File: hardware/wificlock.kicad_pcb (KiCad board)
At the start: 4 copper layers, 71.8 x 30.5 mm, 41 parts, among them J1 USB_C_Receptacle_USB2.0, Q1 AO3402, Q2 AO3402, Q3 AO3402, Q4 AO3402, SW1 SW_SPST, SW2 SW_SPST, SW3 SW_SPST, U1 CH340C/G, U2 ESP-12F, U3 ME6211C33M5G, U4 HT16K33-20SOP, U5 KW4-56NCLB-P, Y1 12MHz

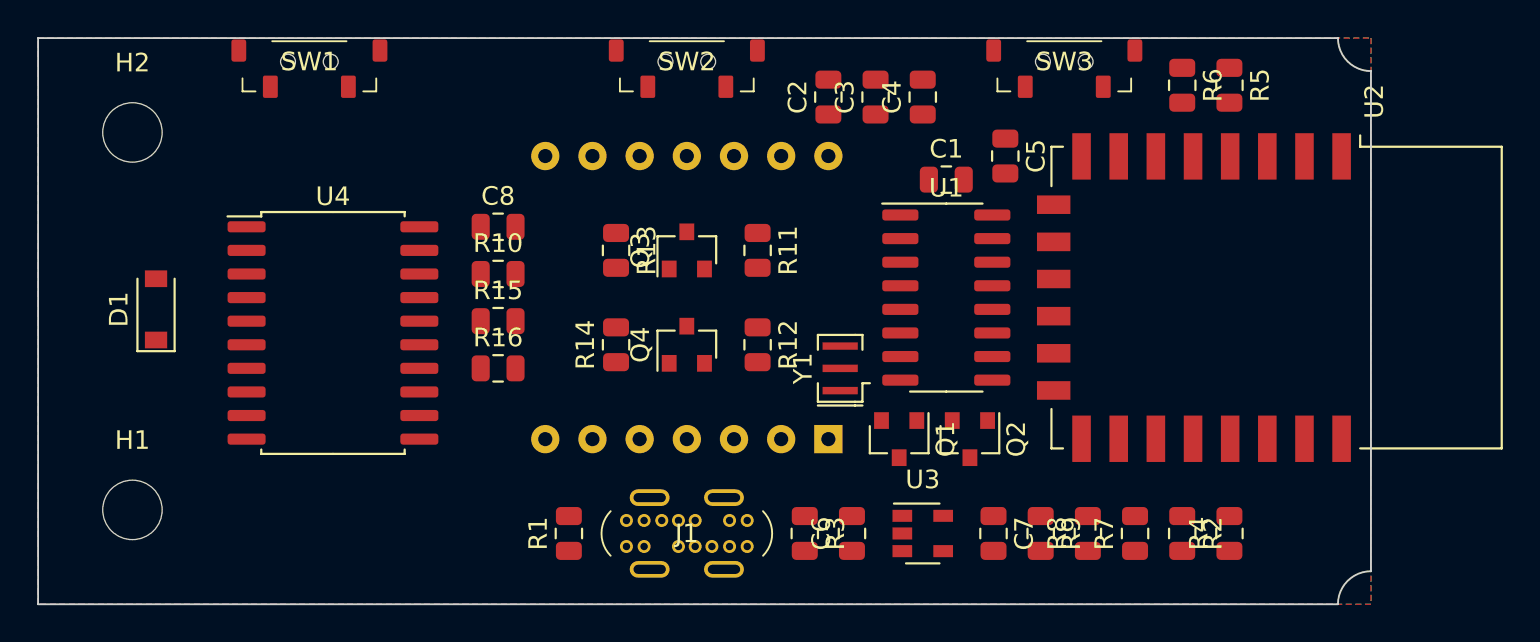
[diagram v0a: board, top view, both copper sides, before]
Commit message: manually route IC decoupling and some other critical traces
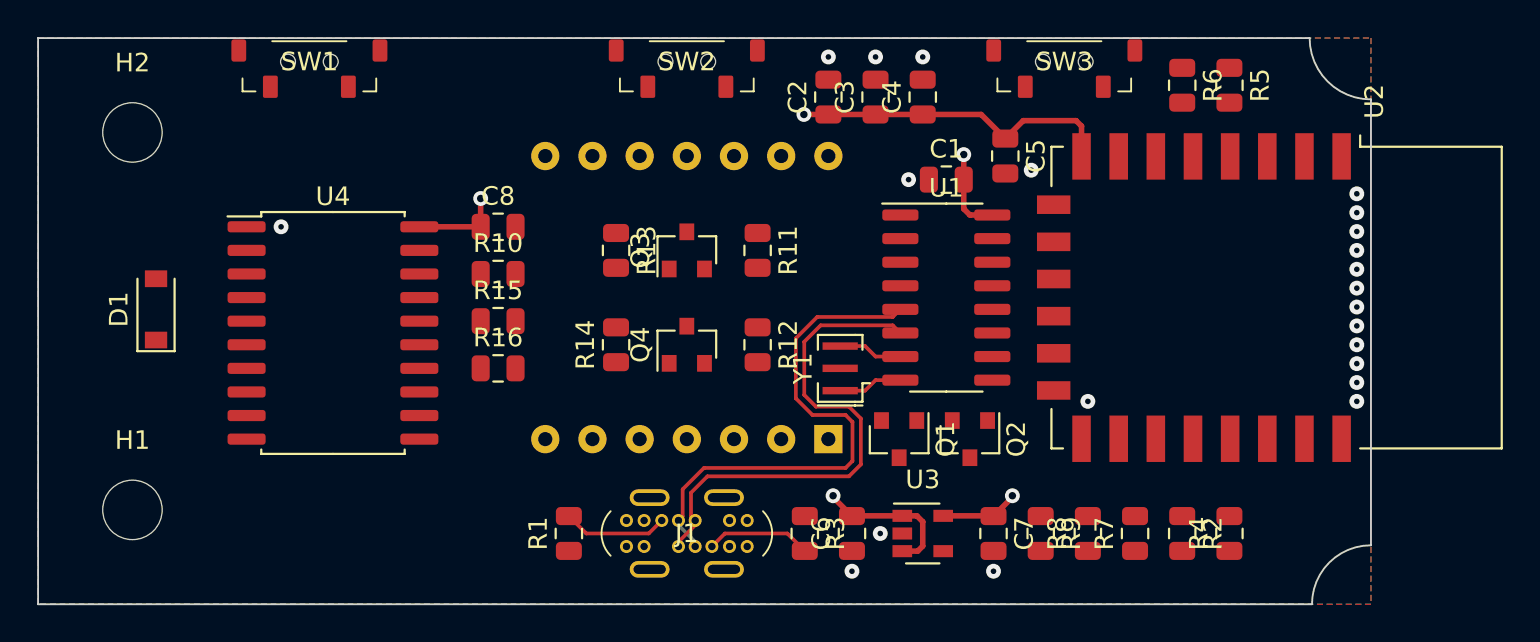
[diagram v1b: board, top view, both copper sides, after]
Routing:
- net D+: track 0.00 -> 28.5 mm
- net D-: track 0.00 -> 27.8 mm
- net +3V3: track 0.00 -> 26.5 mm, vias 0 -> 3
- net +5V: track 0.00 -> 12.8 mm, vias 0 -> 2
- net Net-(J1-PadB5): track 0.00 -> 5.68 mm
- net Net-(J1-PadA5): track 0.00 -> 5.68 mm
- net Net-(U1-Pad8): track 0.00 -> 3.47 mm
- net Net-(U1-Pad7): track 0.00 -> 3.47 mm
- net GND: vias 0 -> 22
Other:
- outline, holes or cut-outs redrawn

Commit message: autoroute and small manual routing fixes
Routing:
- net Net-(D1-Pad1): track 0.00 -> 58.7 mm
- net Net-(R16-Pad2): track 0.00 -> 46.4 mm
- net ~RST: track 0.00 -> 43.4 mm
- net SCL33: track 0.00 -> 39.4 mm, vias 0 -> 2
- net COM1: track 0.00 -> 34.4 mm
- net SDA33: track 0.00 -> 34.0 mm, vias 0 -> 2
- net COM0: track 0.00 -> 33.4 mm
- net K1: track 0.00 -> 30.7 mm, vias 0 -> 2
- net ROW5: track 0.00 -> 28.7 mm, vias 0 -> 1
- net COM2: track 0.00 -> 27.7 mm, vias 0 -> 1
- net ROW7: track 0.00 -> 27.5 mm
- net Net-(R4-Pad1): track 0.00 -> 27.4 mm, vias 0 -> 2
- net Net-(R2-Pad2): track 0.00 -> 25.2 mm, vias 0 -> 2
- net ROW3: track 0.00 -> 24.6 mm, vias 0 -> 1
- net ROW4: track 0.00 -> 23.3 mm
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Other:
- board text added: "WiFiClock V1.0"

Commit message: use correct diode model
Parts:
- D1: value D -> 1N4148W
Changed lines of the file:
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@@
     (visible_elements FFFFE77F)
     (pcbplotparams
-      (layerselection 0x010fc_ffffffff)
+      (layerselection 0x010f0_ffffffff)
       (usegerberextensions false)
       (usegerberattributes true)
@@
     (uvia_drill 0.1)
   )
+  (module Diode_SMD:D_SOD-123 (layer F.Cu)
+    (at 98.425 127.635 90)
+    (descr SOD-123)
+    (tags SOD-123)
+    (attr smd)
+    (fp_text reference D1 (at 0 -2 90) (layer F.SilkS)
+      (effects (font (size 1 1) (thickness 0.15)))
+    )
+    (fp_text value 1N4148W (at 0 2.1 90) (layer F.Fab)
+      (effects (font (size 1 1) (thickness 0.15)))
+    )
+    (fp_text user %R (at 0 -2 90) (layer F.Fab)
+      (effects (font (size 1 1) (thickness 0.15)))
+    )
+    (fp_line (start -2.25 -1) (end -2.25 1) (layer F.SilkS) (width 0.12))
+    (fp_line (start 0.25 0) (end 0.75 0) (layer F.Fab) (width 0.1))
+    (fp_line (start 0.25 0.4) (end -0.35 0) (layer F.Fab) (width 0.1))
+    (fp_line (start 0.25 -0.4) (end 0.25 0.4) (layer F.Fab) (width 0.1))
+    (fp_line (start -0.35 0) (end 0.25 -0.4) (layer F.Fab) (width 0.1))
+    (fp_line (start -0.35 0) (end -0.35 0.55) (layer F.Fab) (width 0.1))
+    (fp_line (start -0.35 0) (end -0.35 -0.55) (layer F.Fab) (width 0.1))
+    (fp_line (start -0.75 0) (end -0.35 0) (layer F.Fab) (width 0.1))
+    (fp_line (start -1.4 0.9) (end -1.4 -0.9) (layer F.Fab) (width 0.1))
+    (fp_line (start 1.4 0.9) (end -1.4 0.9) (layer F.Fab) (width 0.1))
+    (fp_line (start 1.4 -0.9) (end 1.4 0.9) (layer F.Fab) (width 0.1))
+    (fp_line (start -1.4 -0.9) (end 1.4 -0.9) (layer F.Fab) (width 0.1))
+    (fp_line (start -2.35 -1.15) (end 2.35 -1.15) (layer F.CrtYd) (width 0.05))
+    (fp_line (start 2.35 -1.15) (end 2.35 1.15) (layer F.CrtYd) (width 0.05))
+    (fp_line (start 2.35 1.15) (end -2.35 1.15) (layer F.CrtYd) (width 0.05))
+    (fp_line (start -2.35 -1.15) (end -2.35 1.15) (layer F.CrtYd) (width 0.05))
+    (fp_line (start -2.25 1) (end 1.65 1) (layer F.SilkS) (width 0.12))
+    (fp_line (start -2.25 -1) (end 1.65 -1) (layer F.SilkS) (width 0.12))
+    (pad 2 smd rect (at 1.65 0 90) (size 0.9 1.2) (layers F.Cu F.Paste F.Mask)
+      (net 4 COM1))
+    (pad 1 smd rect (at -1.65 0 90) (size 0.9 1.2) (layers F.Cu F.Paste F.Mask)
+      (net 5 "Net-(D1-Pad1)"))
+    (model ${KISYS3DMOD}/Diode_SMD.3dshapes/D_SOD-123.wrl
+      (at (xyz 0 0 0))
+      (scale (xyz 1 1 1))
+      (rotate (xyz 0 0 0))
+    )
+  )
   (module RF_Module:ESP-12E (layer F.Cu)
     (at 158.75 127 270)
@@
       (at (xyz 0 0 0))
       (scale (xyz 1 1 1))
-      (rotate (xyz 0 0 0))
-    )
-  )
-  (module Diode_SMD:D_SOD-123 (layer F.Cu)
-    (at 98.425 127.635 90)
-    (descr SOD-123)
-    (tags SOD-123)
-    (attr smd)
-    (fp_text reference D1 (at 0 -2 90) (layer F.SilkS)
-      (effects (font (size 1 1) (thickness 0.15)))
-    )
-    (fp_text value D (at 0 2.1 90) (layer F.Fab)
-      (effects (font (size 1 1) (thickness 0.15)))
-    )
-    (fp_line (start -2.25 -1) (end -2.25 1) (layer F.SilkS) (width 0.12))
-    (fp_line (start 0.25 0) (end 0.75 0) (layer F.Fab) (width 0.1))
-    (fp_line (start 0.25 0.4) (end -0.35 0) (layer F.Fab) (width 0.1))
-    (fp_line (start 0.25 -0.4) (end 0.25 0.4) (layer F.Fab) (width 0.1))
-    (fp_line (start -0.35 0) (end 0.25 -0.4) (layer F.Fab) (width 0.1))
-    (fp_line (start -0.35 0) (end -0.35 0.55) (layer F.Fab) (width 0.1))
-    (fp_line (start -0.35 0) (end -0.35 -0.55) (layer F.Fab) (width 0.1))
-    (fp_line (start -0.75 0) (end -0.35 0) (layer F.Fab) (width 0.1))
-    (fp_line (start -1.4 0.9) (end -1.4 -0.9) (layer F.Fab) (width 0.1))
-    (fp_line (start 1.4 0.9) (end -1.4 0.9) (layer F.Fab) (width 0.1))
-    (fp_line (start 1.4 -0.9) (end 1.4 0.9) (layer F.Fab) (width 0.1))
-    (fp_line (start -1.4 -0.9) (end 1.4 -0.9) (layer F.Fab) (width 0.1))
-    (fp_line (start -2.35 -1.15) (end 2.35 -1.15) (layer F.CrtYd) (width 0.05))
-    (fp_line (start 2.35 -1.15) (end 2.35 1.15) (layer F.CrtYd) (width 0.05))
-    (fp_line (start 2.35 1.15) (end -2.35 1.15) (layer F.CrtYd) (width 0.05))
-    (fp_line (start -2.35 -1.15) (end -2.35 1.15) (layer F.CrtYd) (width 0.05))
-    (fp_line (start -2.25 1) (end 1.65 1) (layer F.SilkS) (width 0.12))
-    (fp_line (start -2.25 -1) (end 1.65 -1) (layer F.SilkS) (width 0.12))
-    (fp_text user %R (at 0 -2 90) (layer F.Fab)
-      (effects (font (size 1 1) (thickness 0.15)))
-    )
-    (pad 2 smd rect (at 1.65 0 90) (size 0.9 1.2) (layers F.Cu F.Paste F.Mask)
-      (net 4 COM1))
-    (pad 1 smd rect (at -1.65 0 90) (size 0.9 1.2) (layers F.Cu F.Paste F.Mask)
-      (net 5 "Net-(D1-Pad1)"))
-    (model ${KISYS3DMOD}/Diode_SMD.3dshapes/D_SOD-123.wrl
-      (at (xyz 0 0 0))
-      (scale (xyz 1 1 1))

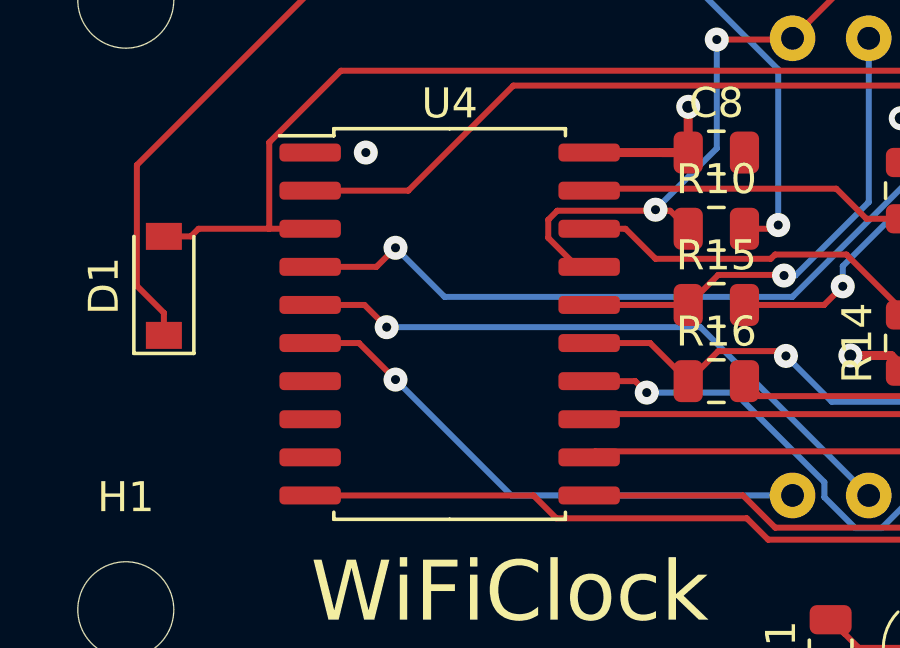
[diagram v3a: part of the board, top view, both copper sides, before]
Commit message: add order number marker for JLCPCB
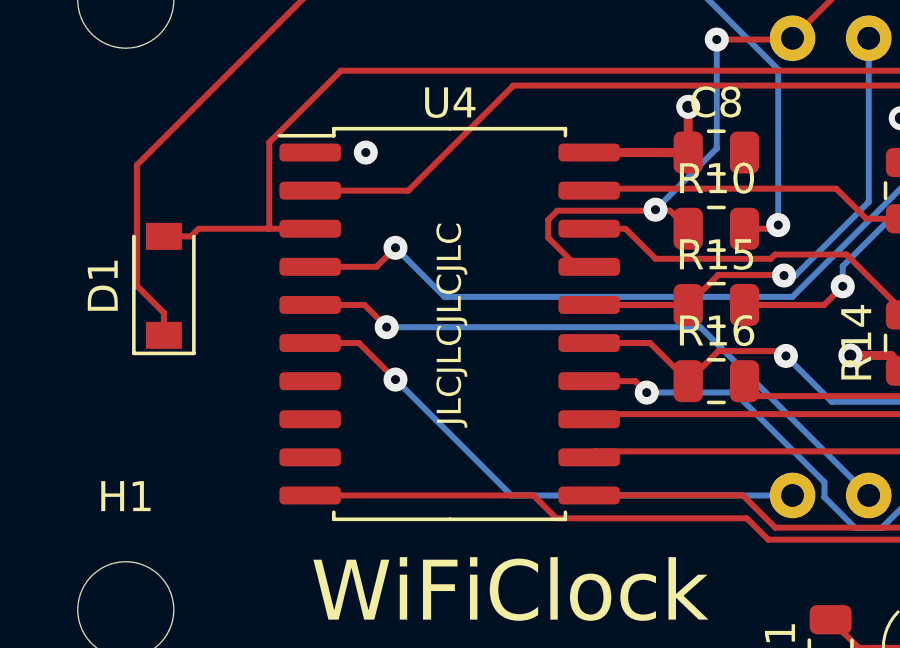
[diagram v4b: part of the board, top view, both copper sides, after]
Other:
- board text added: "JLCJLCJLCJLC"
